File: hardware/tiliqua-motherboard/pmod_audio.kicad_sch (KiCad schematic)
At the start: 1 part, among them J1 Conn_01x15

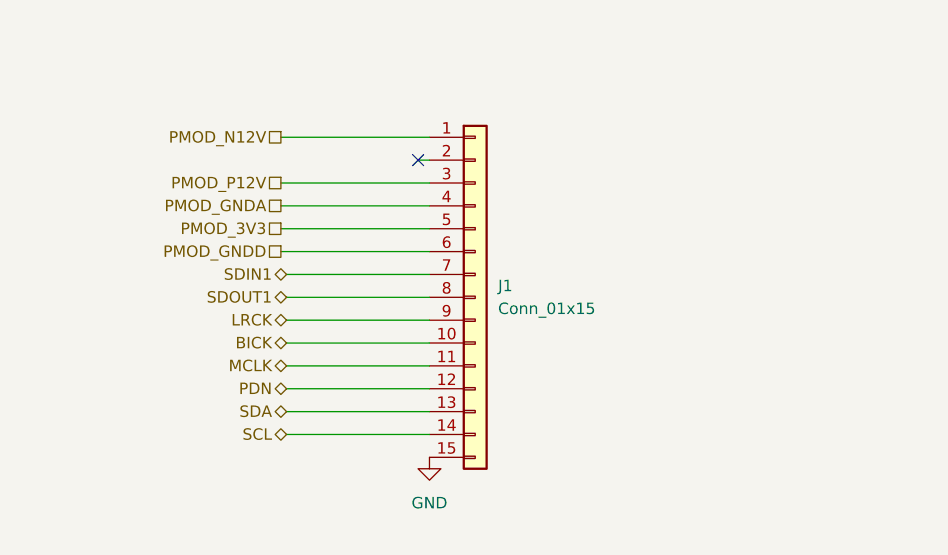
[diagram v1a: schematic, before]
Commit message: schematic cleanup, dual-role usb c
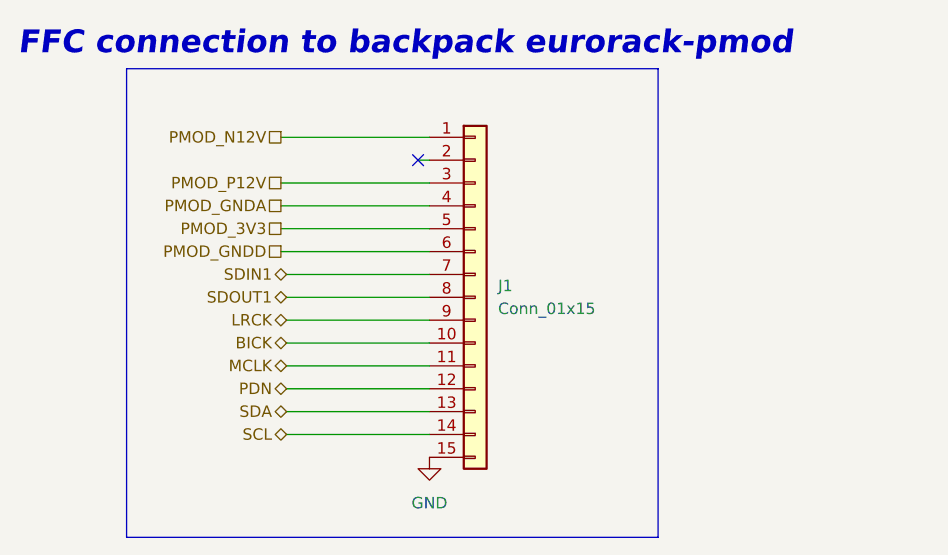
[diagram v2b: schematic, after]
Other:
- note added: "FFC connection to backpack eurorack-pmod"
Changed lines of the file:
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@@
+		)
+	)
+	(rectangle
+		(start 99.695 48.26)
+		(end 158.75 100.33)
+		(stroke
+			(width 0)
+			(type default)
+		)
+		(fill
+			(type none)
+		)
+	)
+	(text "FFC connection to backpack eurorack-pmod"
+		(exclude_from_sim no)
+		(at 87.63 46.99 0)
+		(effects
+			(font
+				(size 2.54 2.54)
+				(thickness 0.508)
+				(bold yes)
+				(italic yes)
+			)
+			(justify left bottom)
 		)
 	)

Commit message: hw/mobo-r3: assign remaining part numbers
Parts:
- J1: lcsc# C5378715 -> C5373472
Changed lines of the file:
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@@
 			)
 		)
-		(property "lcsc#" "C5378715"
+		(property "lcsc#" "C5373472"
 			(at 138.43 73.66 0)
 			(effects

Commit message: hw/mobo-r3: add LCSC database / associations
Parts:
- J1: LCSC (none) -> C5373472
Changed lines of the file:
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@@
+			)
+		)
+		(property "LCSC" "C5373472"
+			(at 140.97 72.3899 0)
+			(effects
+				(font
+					(size 1.27 1.27)
+				)
+				(hide yes)
 			)
 		)
